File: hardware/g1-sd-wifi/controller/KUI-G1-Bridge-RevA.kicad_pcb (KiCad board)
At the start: 6 copper layers, 59 x 105 mm, 349 parts, among them J10 FPGA JTAG pogo pads, J20 5V/GND direct wire pads, J201 microSD push-pull 1.42mm, J202 RP USB service pads, J203 RP SWD/reset/boot pads, J204 C5 direct UART recovery pads, J40 FH12-14S-0.5SH(55), J41 FH12-6S-0.5SH(55), J50 FH12-20S-0.5SH(55), J51 FH12-20S-0.5SH(55), K201 C5 removable compression cont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, K202 C5 removable compression cont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, K203 C5 removable compression cont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, K204 C5 removable compression cont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, K205 C5 removable compression cont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, K206 C5 removable compression cont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, K207 C5 removable compression cont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, K208 C5 removable compression cont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, K209 C5 removable compression cont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, K210 C5 removable compression cont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, K211 C5 removable compression cont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, K212 C5 removable compression cont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, K213 C5 removable compression cont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, K214 C5 removable compression cont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, K215 C5 removable compression cont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, K216 C5 removable compression cont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, Q20 PMV48XP reverse polarity, Q201 C5 recovery pull-down, Q202 C5 recovery pull-down, U10 LCMXO2-2000HC-4TG100C, U20 TPS2116 automatic mux, U201 RP2350B, U202 16MiB boot NOR, U203 8MiB QSPI PSRAM, U204 C5 off-state isolation, U205 C5 off-state isolation, U207 SD4-bit DAT rail isolation, U208 SD CLK/CMD rail isolation, U209 SD enable/power-good NAND, U21 TPS62162 3.3V 1A, U22 TPS62162 3.3V 1A, U23 TPS3808G33DBVR, U24 TPS3808G33DBVR, U25 TPS3808G33DBVR, U26 TPS3808G01DBVR, U27 SN74LVC2G08DCUR, U28 SN74LVC2G08DCUR, U29 SN74LVC2G08DCUR, U30 SN74LVC1G11DBVR, U31 SN74LVC2G04DBVT, U32 SN74LVC1G32DBVR, U33 SN74LVC1G08DBVR, U34 SN74LVC1G08DBVR, U35 SN74LVC16T245, U36 SN74LVC244A host controls, U37 SN74LVC1G17 host RESETn, U38 SN74LVC1G125 qualified ATA_IN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, U39 SN74LVC1G125 qualified ATA_DM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, U40 MX29LV640ETTI-70G x8 / 4 x 2M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, U41 SN74LVC2G125 bank-domain buff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, U42 SN74LVC1G11 write-authorize A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, U43 SN74LVC1G04 write-block inver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, U44 SN74LVC1G332 NOR WE qualifier, U45 TLV803EB29 console-rail NOR r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, U70 SN74LVC1G07 open-drain IORDY, U71 TPS22919 Wi-Fi input switch, U72 SN74LVC1G32DBVR, U73 SN74LVC1G32DBVR, X10 50MHz 3.3V, X201 12MHz

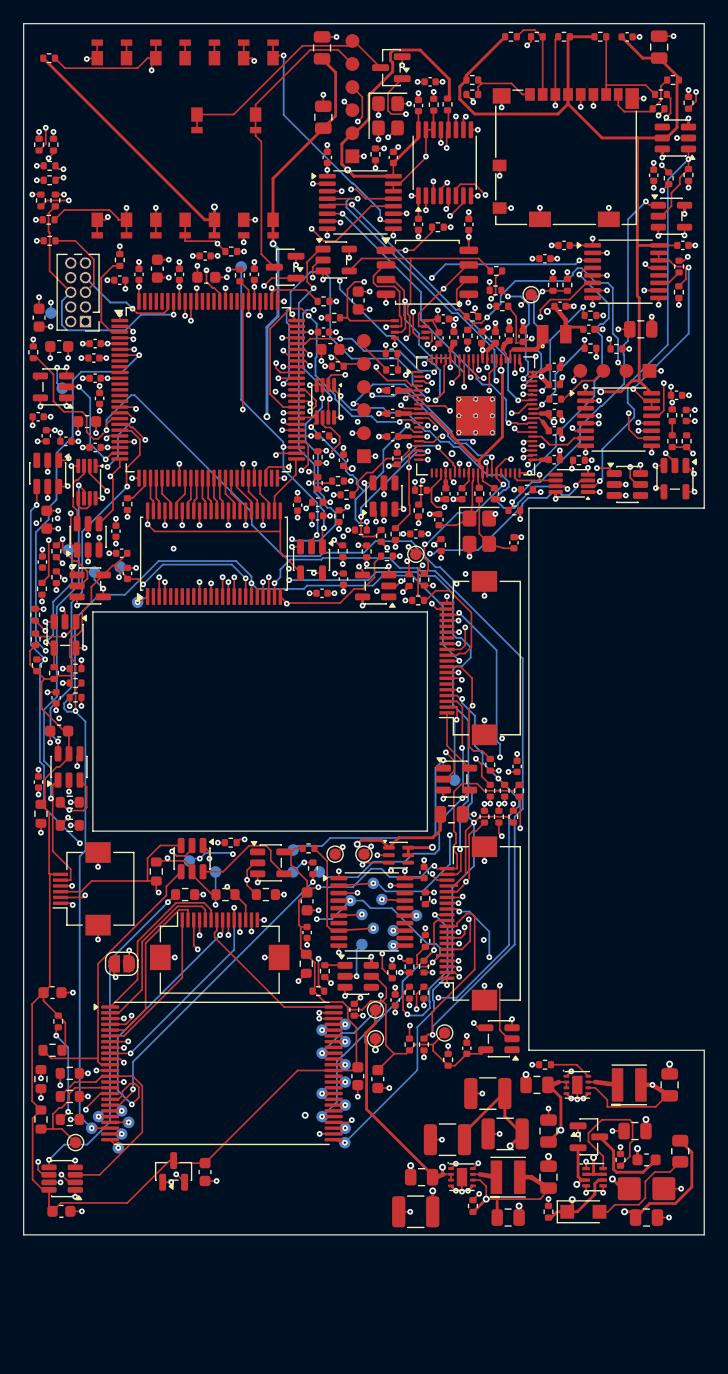
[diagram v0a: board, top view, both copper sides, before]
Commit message: G1 carrier: 59 x 115 mm outline, 10 mm band above the BIOS opening (unrouted)
The 59 x 105 mm board was 76 % full by part area and routing stalled at
30 open connections, all in the corridors beside the BIOS opening. The
floorplan now inserts a 10 mm band between U35 and the opening: the
opening, the CN503 notch, J50/J51 and the south half move south together,
so in motherboard terms the carrier grows 10 mm north and its south edge
stays put. tools/stretch_board.py does the move (edges, zones, rigid
copper islands); outline constants in the placers, router helpers and
fit-template generator follow. All parts placed, total placement wire
length 1711 mm (was 1886), DRC 0, parity 0; routing follows.

The placers also gain --channel keepouts (unused by the floorplan).

Co-Authored-By: Claude Opus 5.5 <noreply@anthropic.com>
Claude-Session: https://claude.ai/code/session_01Gp9EYc2r9fMpZ7V8WtfonZ
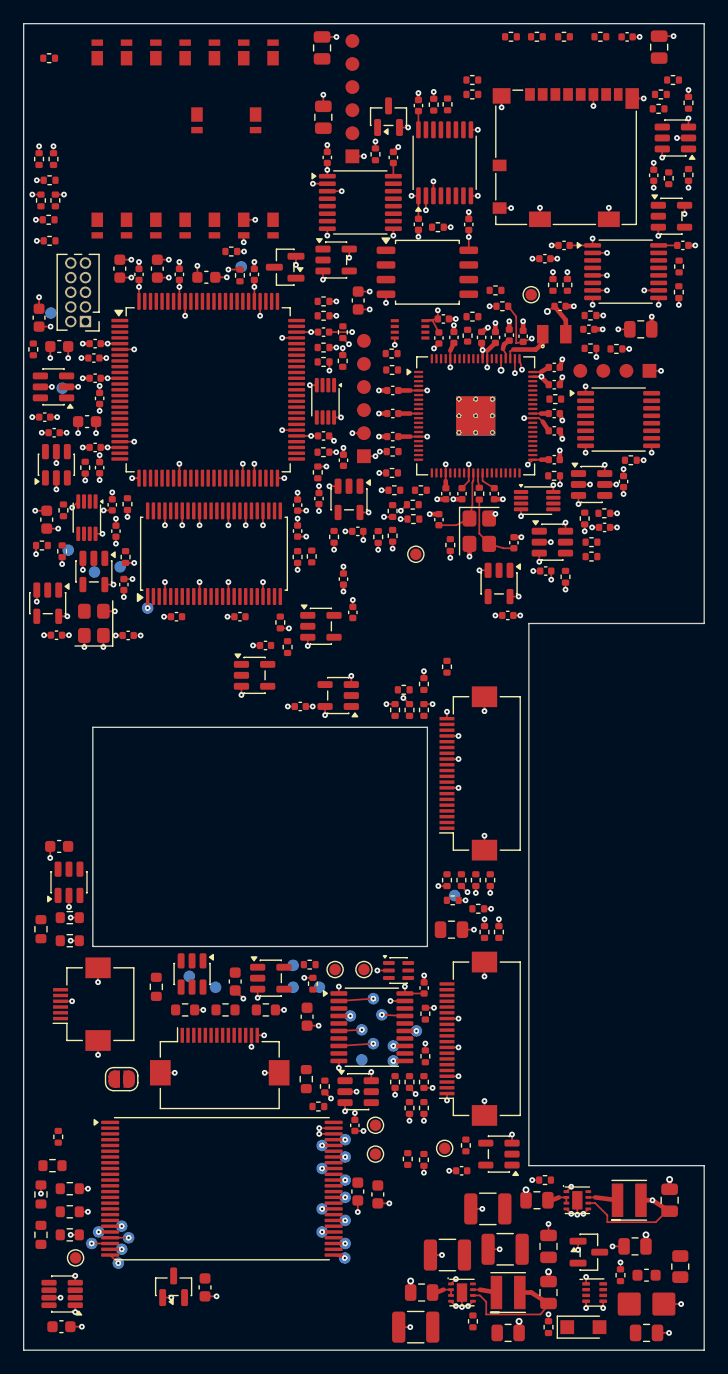
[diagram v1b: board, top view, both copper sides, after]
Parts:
- moved R268 55.8 mm to (108.3, 142.2), turned to -90 degrees
- moved C119 54.7 mm to (79.1, 98.0)
- moved X10 50.9 mm to (76.1, 97.0), turned to 90 degrees
- moved R244 40.4 mm to (110.5, 119.2), turned to -90 degrees
- moved R252 30.2 mm to (104.7, 102.2), turned to 90 degrees
- moved R265 29.5 mm to (95.0, 91.2), turned to -90 degrees
- moved C212 27.9 mm to (122.0, 84.7), turned to 90 degrees
- moved R248 27.8 mm to (102.2, 104.5), turned to 90 degrees
- moved C221 27.3 mm to (99.0, 89.0)
- moved C233 27.3 mm to (98.5, 96.0)
- moved R106 26.0 mm to (96.0, 74.3), turned to 180 degrees
- moved R242 25.2 mm to (102.2, 136.8), turned to -90 degrees
- moved C231 25.1 mm to (91.0, 98.9), turned to 180 degrees
- moved C218 24.9 mm to (77.7, 86.7), turned to 90 degrees
- moved C223 24.0 mm to (112.0, 96.3)
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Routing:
- net CONSOLE_3V3: track 274.4 -> 0.00 mm, vias 7 -> 0
- net +3V3_STORAGE: track 187.8 -> 12.8 mm, vias 4 -> 0
- net ATA_DD15: track 110.0 -> 1.00 mm, vias 3 -> 1
- net BIOS_BANK1: track 107.1 -> 0.00 mm, vias 5 -> 0
- net ATA_DD10: track 102.2 -> 1.00 mm, vias 4 -> 1
- net ATA_DD14: track 97.1 -> 1.00 mm, vias 7 -> 1
- net PWR_FAILn: track 94.8 -> 0.00 mm, vias 6 -> 0
- net ATA_DD12: track 95.1 -> 1.60 mm, vias 4 -> 1
- net ATA_DD9: track 90.7 -> 1.00 mm, vias 4 -> 1
- net +5V_C5: track 87.4 -> 0.00 mm, vias 3 -> 0
- net IORDY_RELEASE: track 85.7 -> 0.00 mm, vias 6 -> 0
- net PRIMARY_5V: track 84.4 -> 0.00 mm, vias 4 -> 0
- net BIOS_BANK0: track 83.8 -> 0.00 mm, vias 4 -> 0
- net BUS_SAFE: track 80.9 -> 0.00 mm, vias 5 -> 0
- net INTRQ_OEn: track 80.7 -> 0.00 mm, vias 2 -> 0
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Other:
- board size 59 x 105 mm -> 59 x 115 mm

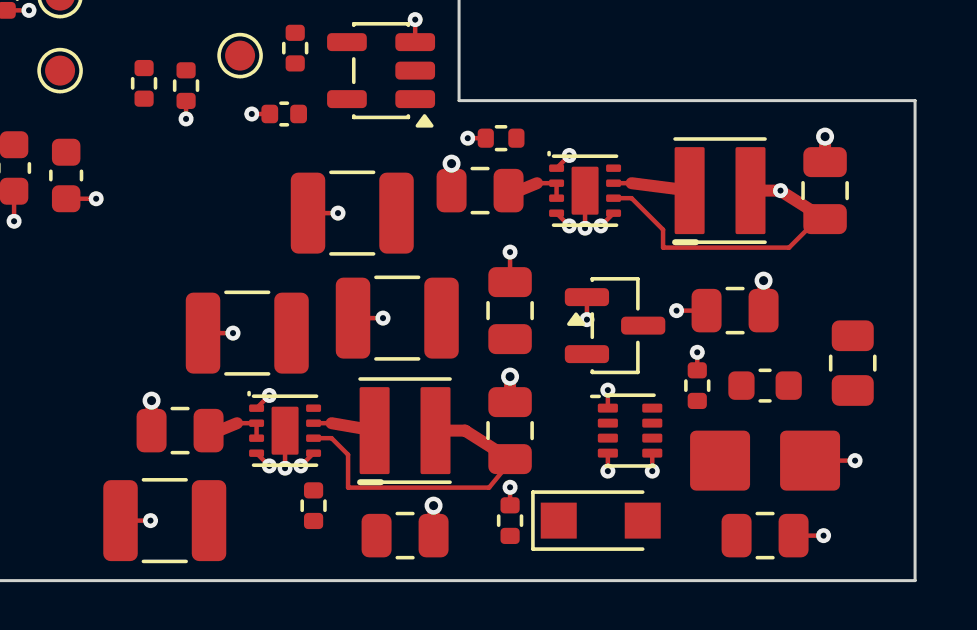
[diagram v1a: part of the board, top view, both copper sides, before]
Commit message: G1 carrier: D21 input TVS turns a 12-V mis-wire into a blown F20
A bidirectional 5-V TVS (SMF5.0CA, SOD-123FL) from FUSED_5V to GND,
between F20 and Q20: above about 6.4 V it conducts far more than F20's
1.5 A rating, so a wrong 12-V feed opens the fuse instead of sitting on
the 5-V parts. Bidirectional, so a reversed 5-V feed stays below
breakdown and Q20 blocks it without blowing F20. Downstream parts may
still see the ~9 V clamp while F20 clears; the doc says so.

Schematic, netlist, ERC (0), integration audit (361 parts) and parts
list regenerated. Its datasheet and JLC catalog identity could not be
reached from this environment, so the part is listed sourcing-pending.
The floorplan places D21 2.2 mm from F20's output; the netlist updater
can now add a part whose footprint is not on the board yet. The power
doc also notes that F20 does not protect the harness itself.

Co-Authored-By: Claude Opus 5.5 <noreply@anthropic.com>
Claude-Session: https://claude.ai/code/session_01Gp9EYc2r9fMpZ7V8WtfonZ
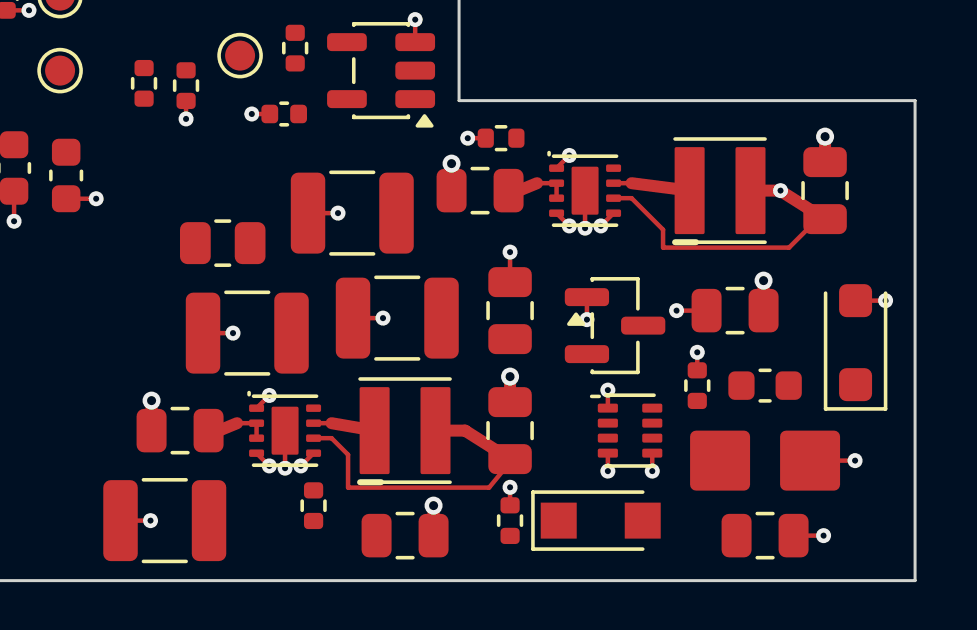
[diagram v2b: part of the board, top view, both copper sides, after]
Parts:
- added D21: 5 V bidirectional TVS, KUI_Footprints:D_SOD-123F, F.Cu at (127.0, 152.1)
- moved R202 21.4 mm to (105.9, 148.8), turned to 0 degrees
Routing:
- net GND: track 219.4 -> 220.4 mm, vias 266 -> 267

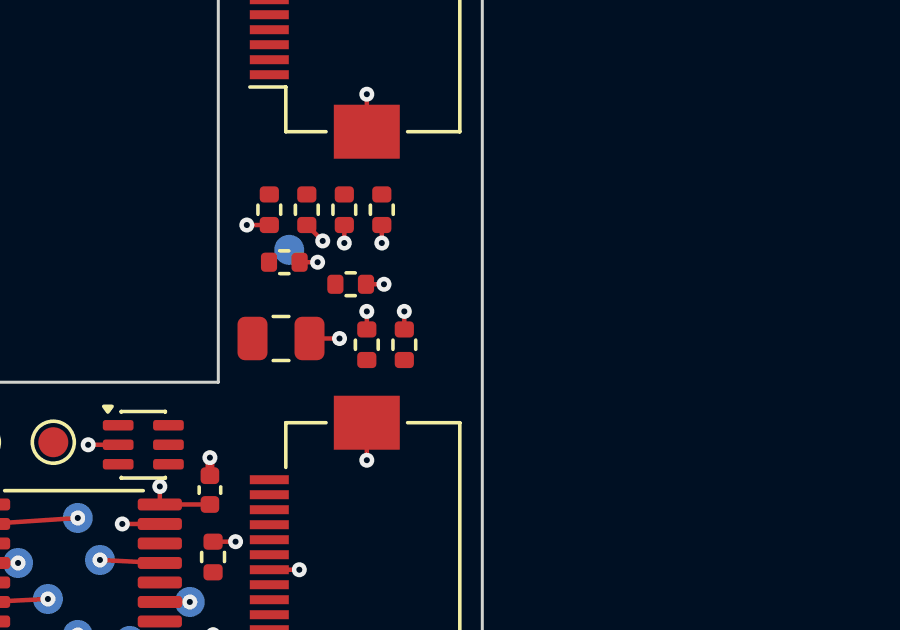
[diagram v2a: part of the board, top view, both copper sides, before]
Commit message: G1 safety: fuse the host 3.3-V entry; no console 5 V on the flex or carrier
Host 3.3 V reached about 30 carrier parts straight from two flex contacts,
and the two console-5-V contacts were joined by an unused carrier trace;
a short on either would load a console supply through 0.5 A connector
contacts with no fuse anywhere. Now:

- F21 (0467.500NR, 0.5 A fast, same 467 family as F20) sits between the one
  remaining 3.3-V entry, J51 B1, and CONSOLE_3V3. If it opens the buffers
  lose VCCB and isolate, and U25 reports the host rail absent.
- CN503 A1 (second 3.3 V) and A3/B3 (5 V) get no flex copper at all: no
  landing pad, no trace, only an unconnected mating finger, so a chafed
  flex cannot short a console supply. Their carrier socket pins are bare.
  flex-interface.json lists them; the flex and carrier generators and both
  checks read that list. Flex ERC/DRC/parity 0; carrier ERC 0, integration
  check pass (362 parts).
- The DSN export keeps the 5-V and storage supply nets on the 1 oz outer
  layers: on 0.5 oz inner copper a 0.25 mm track at the fuse current would
  overheat (IPC-2221).
- F21 is placed by the floorplan next to J51; board DRC 0, parity 0
  (unrouted).

Co-Authored-By: Claude Opus 5.5 <noreply@anthropic.com>
Claude-Session: https://claude.ai/code/session_01Gp9EYc2r9fMpZ7V8WtfonZ
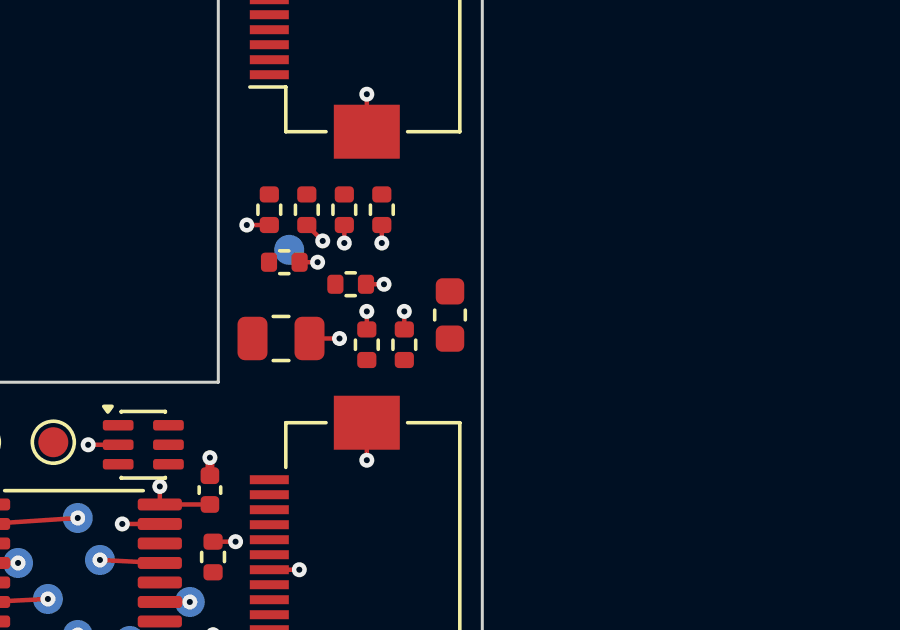
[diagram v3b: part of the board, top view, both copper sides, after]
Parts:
- added F21: 0.5A fast fuse, KUI_Footprints:Fuse_0603_1608Metric, F.Cu at (112.7, 122.8)
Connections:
- J50 pad 1: CONSOLE_3V3 -> unconnected-(J50-A1-Pad1)
- J50 pad 3: FLEX_5V -> unconnected-(J50-A3-Pad3)
- J51 pad 19: FLEX_5V -> unconnected-(J51-B3-Pad19)
- J51 pad 20: CONSOLE_3V3 -> CONSOLE_3V3_FLEX

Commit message: G1 carrier: power-return and regulator thermal vias in the floorplan
J20's ground pad carries the board's whole 5-V return but entered the
plane through one 0.2 mm via; it now has four locked 0.3/0.6 mm vias.
The two TPS62162 exposed pads had none; each gets two locked 0.2/0.5 mm
vias. tools/add_power_vias.py places the grid inside the pad; the
floorplan runs it after fanout. DRC 0, parity 0 (unrouted).

Co-Authored-By: Claude Opus 5.5 <noreply@anthropic.com>
Claude-Session: https://claude.ai/code/session_01Gp9EYc2r9fMpZ7V8WtfonZ
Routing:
- net GND: vias 267 -> 275
